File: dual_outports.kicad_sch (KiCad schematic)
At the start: 20 parts, among them J801 USB_A, J802 USB_A, SW801 SW_Push, SW802 SW_Push, U801 MIC2026-1xM, U802 SRV05-4, U803 74LVC2G08

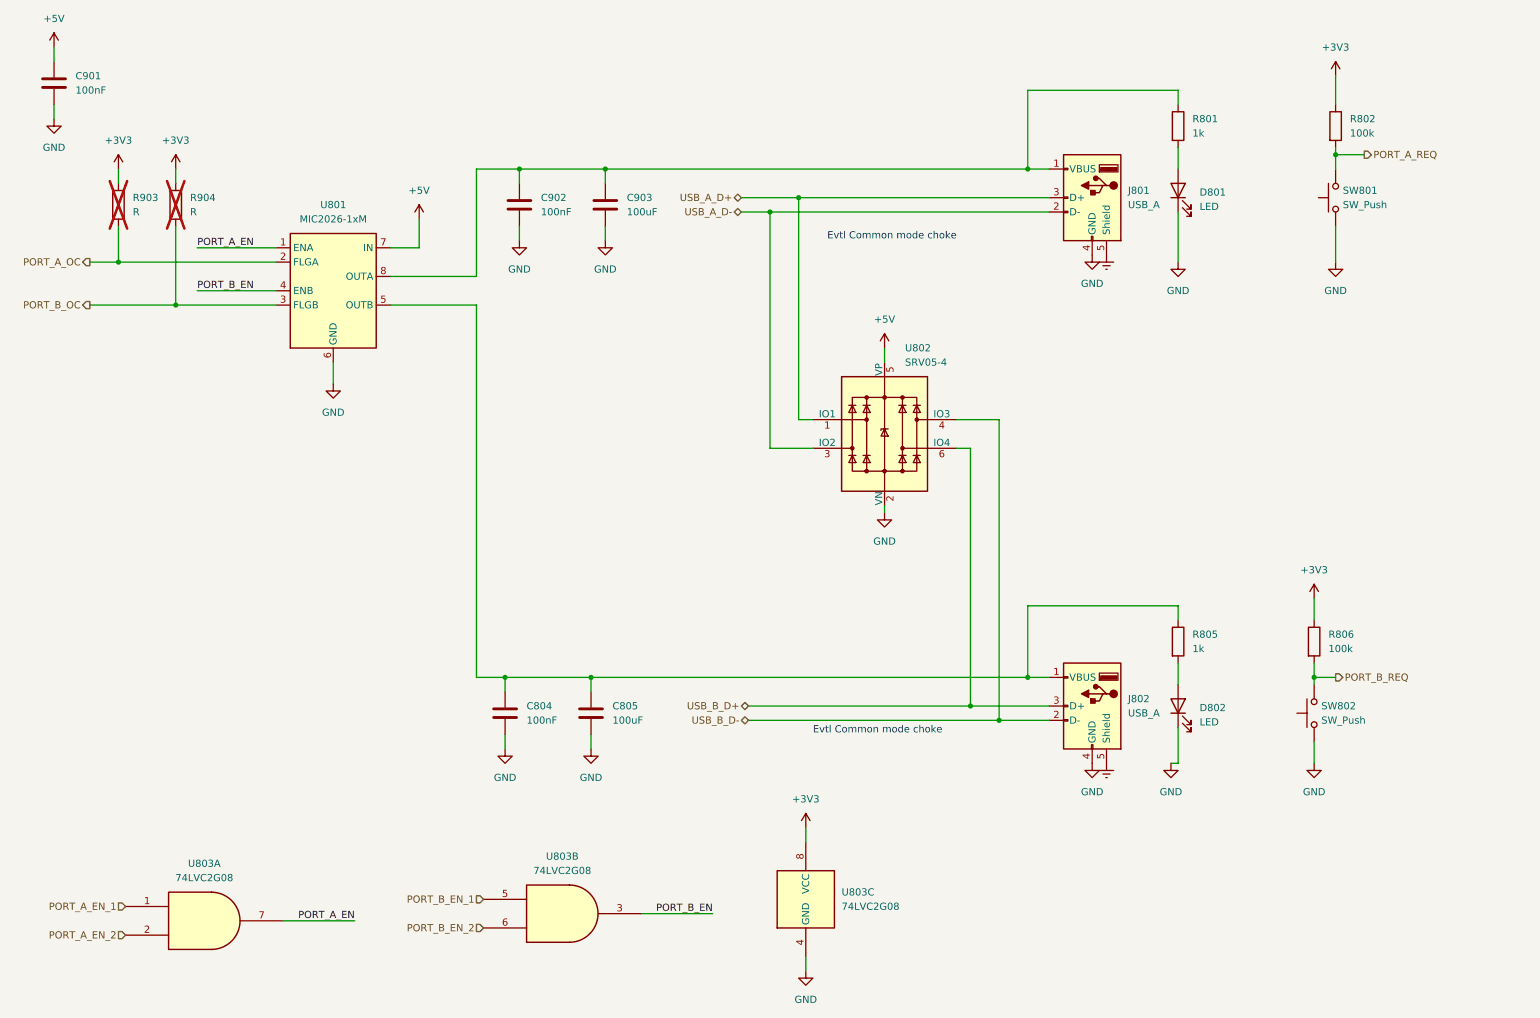
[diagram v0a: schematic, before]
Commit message: Add power management
And also some random stuff here and there
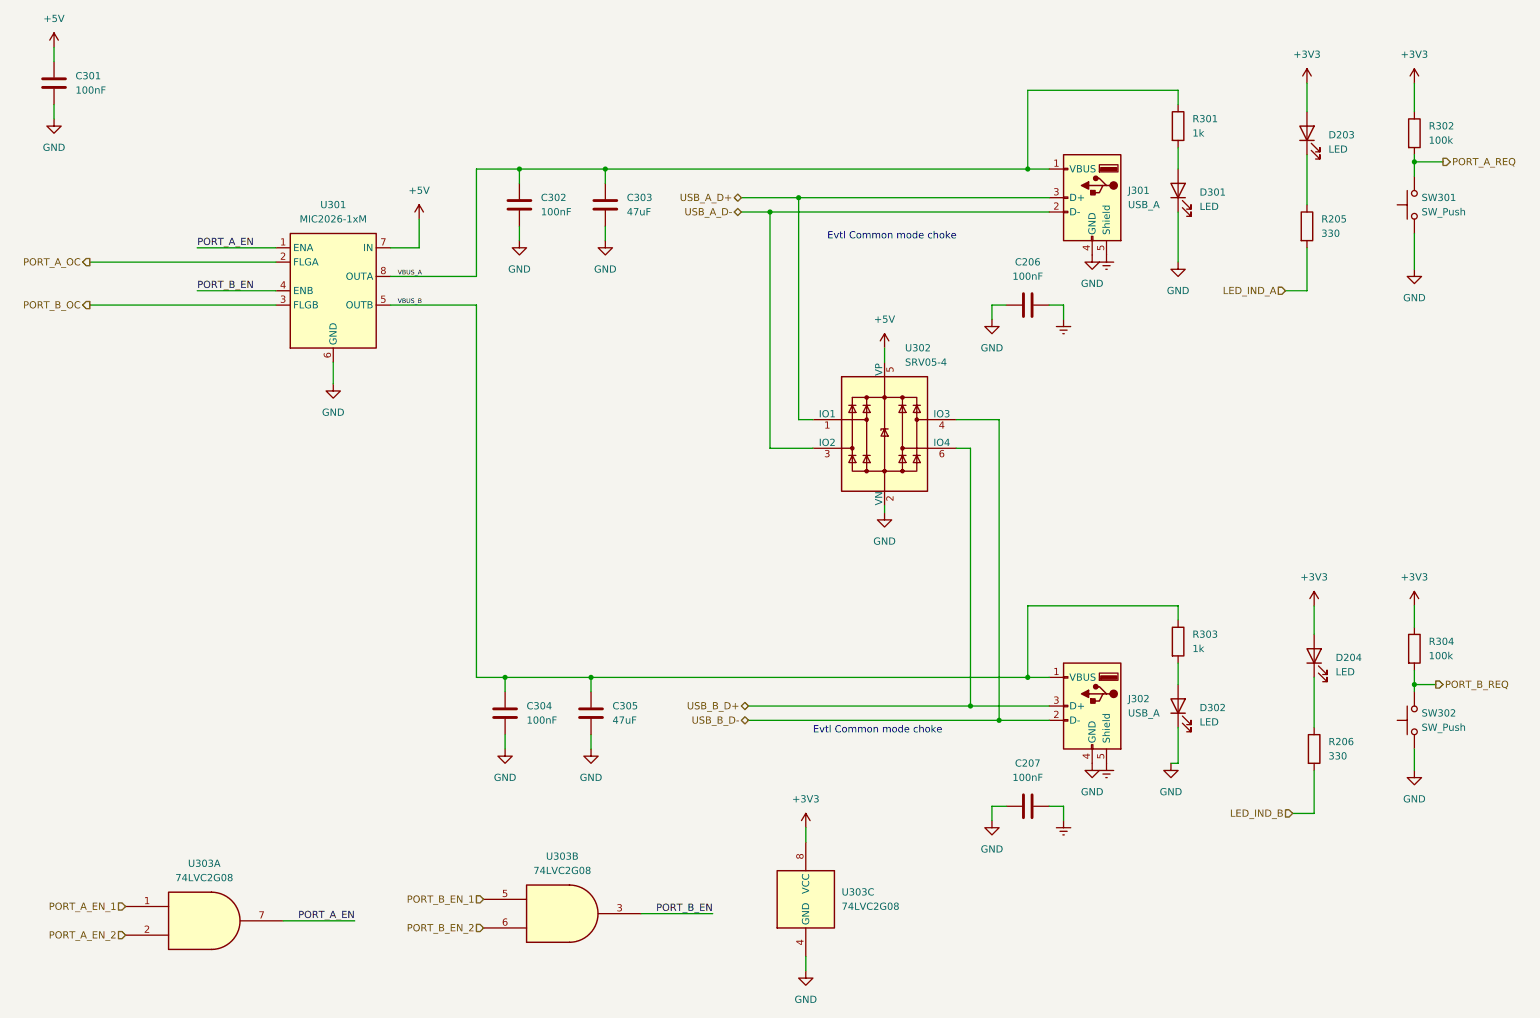
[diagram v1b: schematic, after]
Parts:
- removed R903, R904: R, Resistor_SMD:R_0603_1608Metric, symbol Device:R
- added C206, C207: 100nF, Capacitor_SMD:C_0402_1005Metric, symbol Device:C
- added D203, D204: LED, LED_SMD:LED_0603_1608Metric, symbol Device:LED
- added R205, R206: 330, Resistor_SMD:R_0402_1005Metric, symbol Device:R
- C303: renamed from C903; value 100uF -> 47uF; footprint Capacitor_SMD:C_0402_1005Metric -> Resistor_SMD:R_0805_2012Metric; LCSC# (none) -> C16780
- C305: renamed from C805; value 100uF -> 47uF; footprint Capacitor_SMD:C_0402_1005Metric -> Resistor_SMD:R_0805_2012Metric; LCSC# (none) -> C16780
- renumbered C901 to C301, C902 to C302, C804 to C304, D801 to D301, D802 to D302, J801 to J301, J802 to J302, R801 to R301, R802 to R302, R805 to R303, R806 to R304, SW801 to SW301, SW802 to SW302, U801 to U301, U802 to U302, U803 to U303
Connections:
- net +3V3: now also D203.2 (A), D204.2 (A)
- net Earth: now also C206.2, C207.2
- net GND: now also C206.1, C207.1
- net VBUS_B: now reaches C304.1, C305.1, J302.1 (VBUS), R303.1, U301.5 (OUTB)
- net VBUS_A: now reaches C302.1, C303.1, J301.1 (VBUS), R301.1, U301.8 (OUTA)
- new net: D204.1 (K), R206.1
- new net: D203.1 (K), R205.1
- new net LED_IND_A: R205.2
- new net LED_IND_B: R206.2
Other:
- title: (none) -> Switchable USB Hub
- moved on the sheet: R302, R304, SW301, SW302

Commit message: Refine connectors and overall shape
Replace USB connectors, because of availability.
Use available barrel jack and USB-C connector instead of generic ones.
Update 3D Models

Refine rough placement of parts and board outline
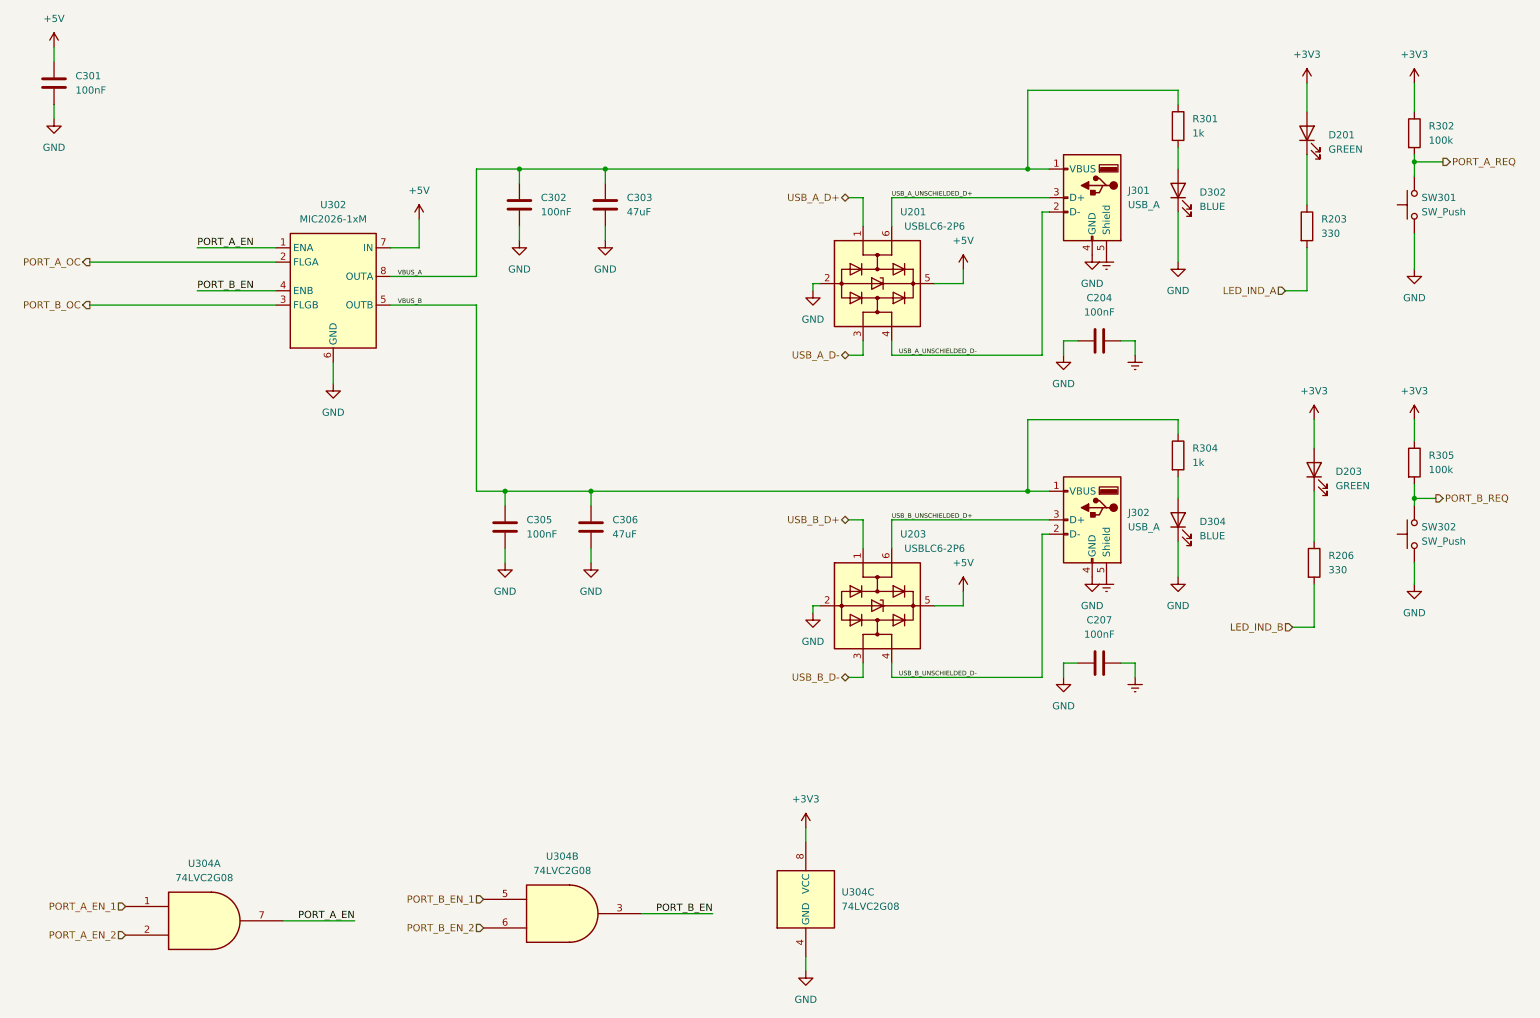
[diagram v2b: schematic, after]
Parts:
- removed U302: SRV05-4, Package_TO_SOT_SMD:SOT-23-6, symbol Power_Protection:SRV05-4
- added U201, U203: USBLC6-2P6, Package_TO_SOT_SMD:SOT-666, symbol Power_Protection:USBLC6-2P6
- C204: renamed from C206; LCSC# (none) -> C307331
- C207, C301, C302: LCSC# (none) -> C307331
- C303: footprint Resistor_SMD:R_0805_2012Metric -> Capacitor_SMD:C_0805_2012Metric
- C305: renamed from C304; LCSC# (none) -> C307331
- C306: renamed from C305; footprint Resistor_SMD:R_0805_2012Metric -> Capacitor_SMD:C_0805_2012Metric
- D201: renamed from D203; value LED -> GREEN; LCSC# (none) -> C2986059
- D203: renamed from D204; value LED -> GREEN; LCSC# (none) -> C2986059
- D302: renamed from D301; value LED -> BLUE; LCSC# (none) -> C72041
- D304: renamed from D302; value LED -> BLUE; LCSC# (none) -> C72041
- J301, J302: footprint Connectors:CU01SAV1S00 -> Connectors:UJ2-AV-W4-TH; LCSC# (none) -> -; MPN (none) -> UJ2-AV-W4-TH; Manufactorer (none) -> CUI Devices
- R203: renamed from R205; LCSC# (none) -> C25104; MPN (none) -> 330R
- R206: LCSC# (none) -> C25104; MPN (none) -> 330R
- R301: LCSC# (none) -> C11702; MPN (none) -> 1k
- R302: LCSC# (none) -> C25741; MPN (none) -> 100K
- R304: renamed from R303; LCSC# (none) -> C11702; MPN (none) -> 1k
- R305: renamed from R304; LCSC# (none) -> C25741; MPN (none) -> 100K
- SW301, SW302: LCSC# (none) -> C318884
- U302: renamed from U301; LCSC# (none) -> C144190; MPN (none) -> MIC2026-1YM
- U304: renamed from U303; MPN (none) -> 74LVC2G08
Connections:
- net +5V: now also U201.5 (VBUS), U203.5 (VBUS)
- net GND: now also U201.2 (GND), U203.2 (GND)
- net USB_A_D+: now also U201.1 (I/O1); no longer J301.3 (D+)
- net USB_A_D-: now also U201.3 (I/O2); no longer J301.2 (D-)
- net USB_B_D+: now also U203.1 (I/O1); no longer J302.3 (D+)
- net USB_B_D-: now also U203.3 (I/O2); no longer J302.2 (D-)
- new net USB_A_UNSCHIELDED_D+: J301.3 (D+), U201.6 (I/O1)
- new net USB_A_UNSCHIELDED_D-: J301.2 (D-), U201.4 (I/O2)
- new net USB_B_UNSCHIELDED_D+: J302.3 (D+), U203.6 (I/O1)
- new net USB_B_UNSCHIELDED_D-: J302.2 (D-), U203.4 (I/O2)
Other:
- note removed: "Evtl Common mode choke"
- moved on the sheet: C204, C207, C305, C306, D203, D304, J302, R206, R304, R305, SW302

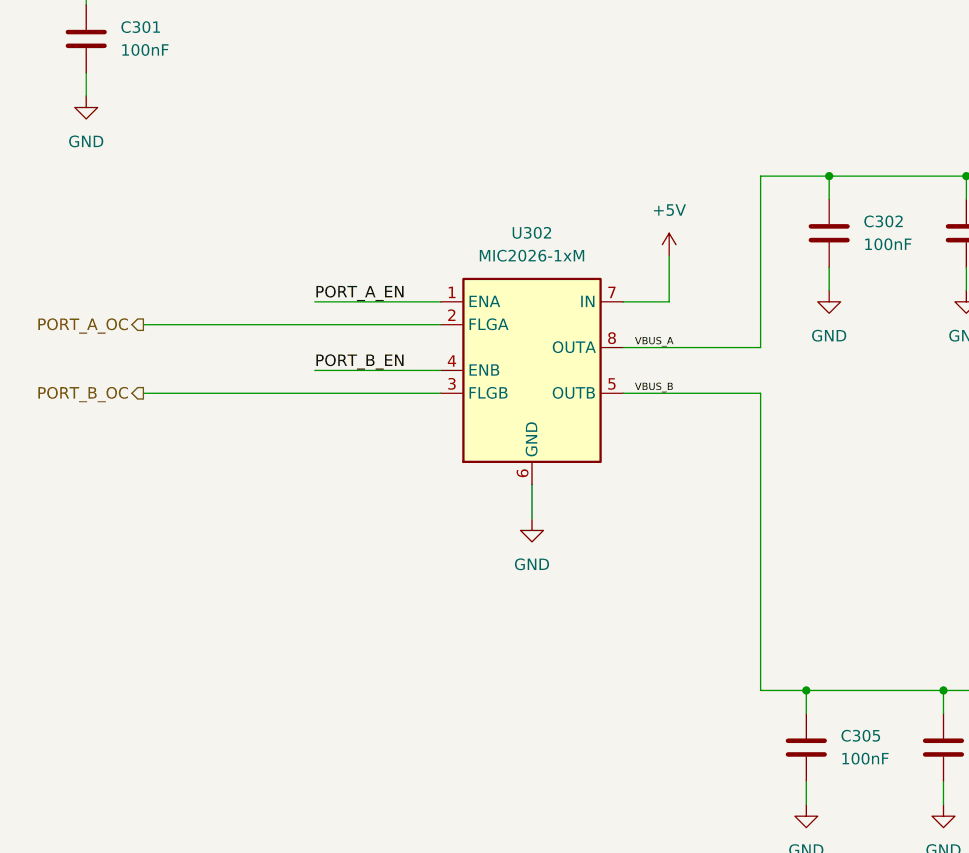
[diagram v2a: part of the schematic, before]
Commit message: Add preliminary routing
Add routing for power paths - 3.3V, 5V and Input power

Add routing close to USB-Ports

Mising routing for main IC's and differntial pair routing
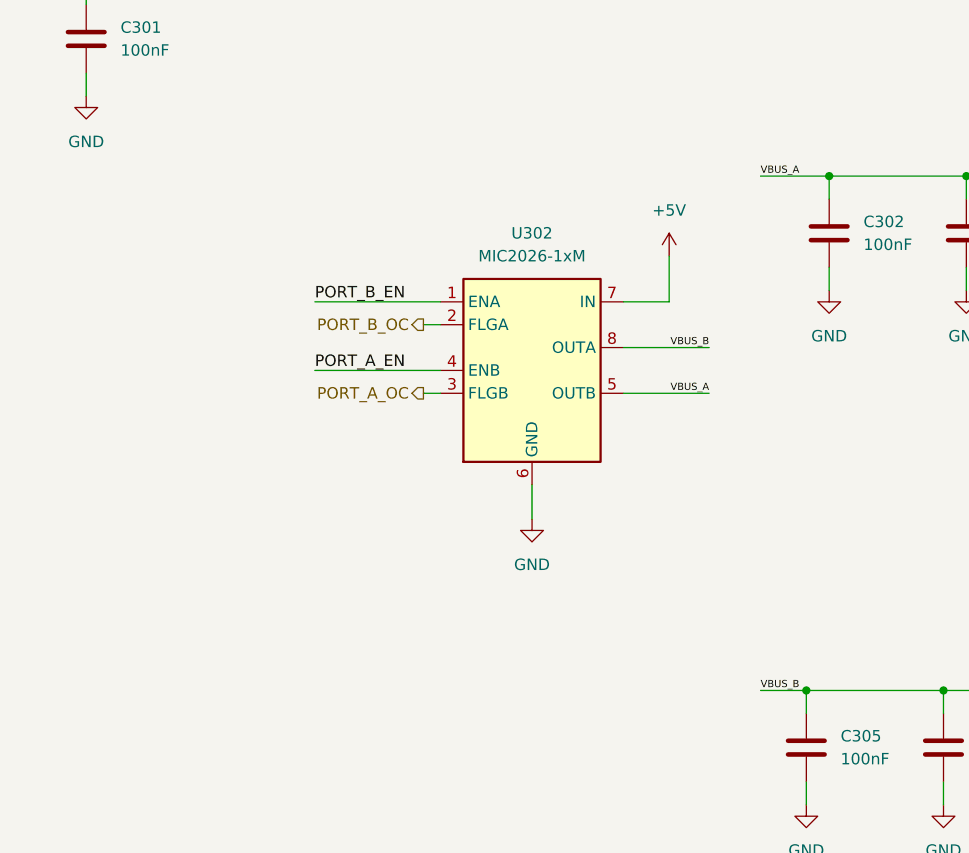
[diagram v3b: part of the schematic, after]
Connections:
- net PORT_A_EN: now also U302.4 (ENB); no longer U302.1 (ENA)
- net PORT_A_OC: now also U302.3 (FLGB); no longer U302.2 (FLGA)
- net PORT_B_EN: now also U302.1 (ENA); no longer U302.4 (ENB)
- net PORT_B_OC: now also U302.2 (FLGA); no longer U302.3 (FLGB)
- net VBUS_A: now also U302.5 (OUTB); no longer U302.8 (OUTA)
- net VBUS_B: now also U302.8 (OUTA); no longer U302.5 (OUTB)

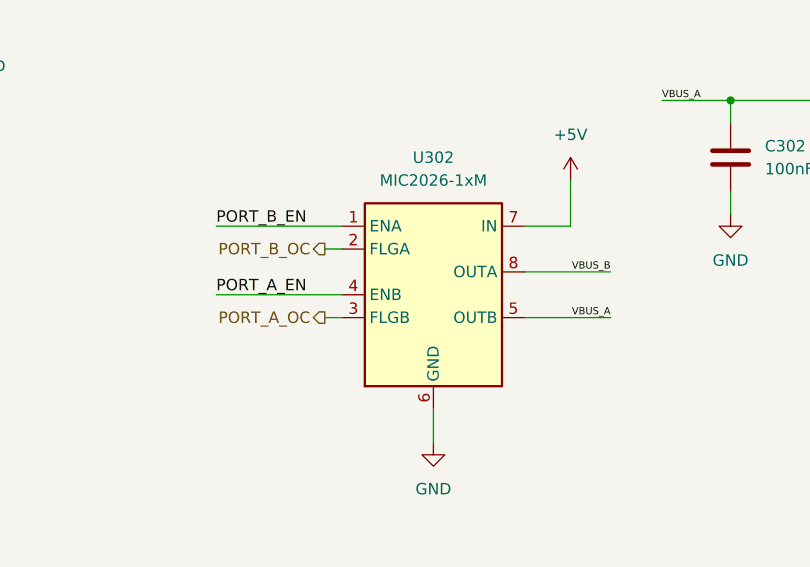
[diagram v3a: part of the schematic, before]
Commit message: Finish first routing
Routed everything, so that the DRC and ERC do not show anything.
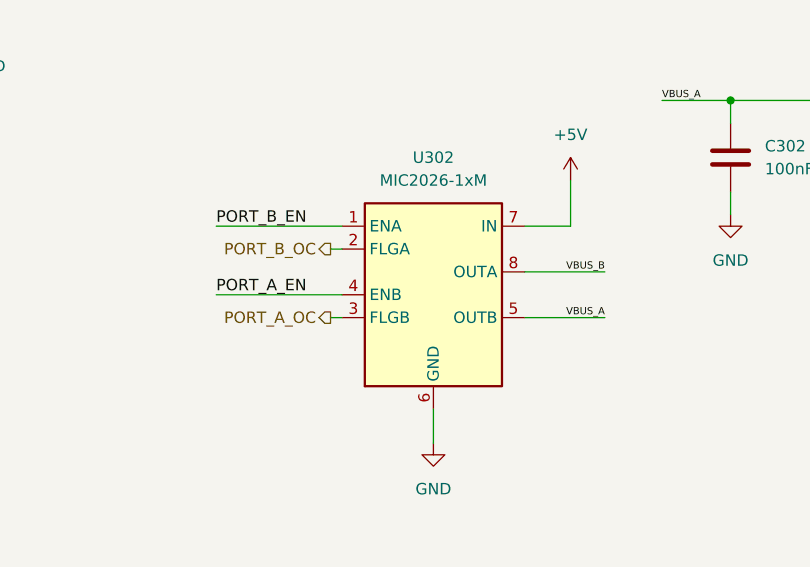
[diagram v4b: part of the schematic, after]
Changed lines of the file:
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@@
     (stroke (width 0) (type default))
   )
-  (wire (pts (xy 59.055 58.42) (xy 60.96 58.42))
+  (wire (pts (xy 59.69 58.42) (xy 60.96 58.42))
     (stroke (width 0) (type default))
   )
@@
     (stroke (width 0) (type default))
   )
-  (wire (pts (xy 81.28 60.96) (xy 90.805 60.96))
+  (wire (pts (xy 81.28 60.96) (xy 90.17 60.96))
     (stroke (width 0) (type default))
   )
@@
     (stroke (width 0) (type default))
   )
-  (wire (pts (xy 59.055 66.04) (xy 60.96 66.04))
+  (wire (pts (xy 59.69 66.04) (xy 60.96 66.04))
     (stroke (width 0) (type default))
   )
@@
     (stroke (width 0) (type default))
   )
-  (wire (pts (xy 81.28 66.04) (xy 90.805 66.04))
+  (wire (pts (xy 81.28 66.04) (xy 90.17 66.04))
     (stroke (width 0) (type default))
   )
@@
     (effects (font (size 1.27 1.27)) (justify right bottom))
   )
-  (label "VBUS_A" (at 90.805 66.04 180) (fields_autoplaced)
+  (label "VBUS_A" (at 90.17 66.04 180) (fields_autoplaced)
     (effects (font (size 0.8 0.8)) (justify right bottom))
   )
@@
     (effects (font (size 1.27 1.27)) (justify right bottom))
   )
-  (label "VBUS_B" (at 90.805 60.96 180) (fields_autoplaced)
+  (label "VBUS_B" (at 90.17 60.96 180) (fields_autoplaced)
     (effects (font (size 0.8 0.8)) (justify right bottom))
   )
@@
     (effects (font (size 1.27 1.27)) (justify right))
   )
-  (hierarchical_label "PORT_A_OC" (shape output) (at 59.055 66.04 180) (fields_autoplaced)
+  (hierarchical_label "PORT_A_OC" (shape output) (at 59.69 66.04 180) (fields_autoplaced)
     (effects (font (size 1.27 1.27)) (justify right))
   )
@@
     (effects (font (size 1.27 1.27)) (justify right))
   )
-  (hierarchical_label "PORT_B_OC" (shape output) (at 59.055 58.42 180) (fields_autoplaced)
-    (effects (font (size 1.27 1.27)) (justify right))
-  )
+  (hierarchical_label "PORT_B_OC" (shape output) (at 59.69 58.42 180) (fields_autoplaced)
+    (effects (font (size 1.27 1.27)) (justify right))
+  )
